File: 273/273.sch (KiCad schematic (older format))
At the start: 3 parts, among them J1 Conn_01x10_Male, J2 Conn_01x10_Male, U1 74HC273

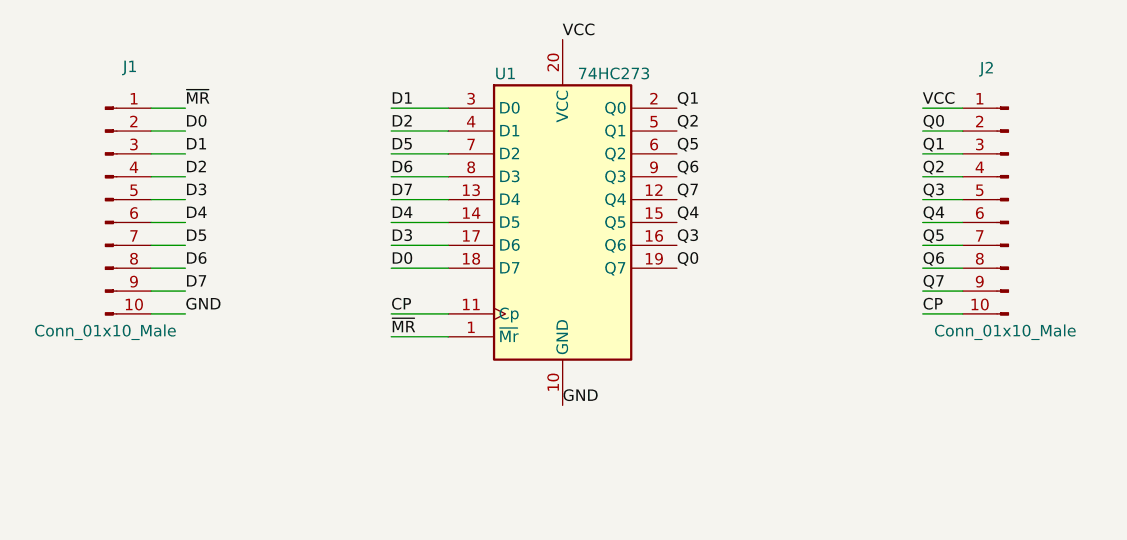
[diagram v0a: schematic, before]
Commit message: Add cap & pull-up
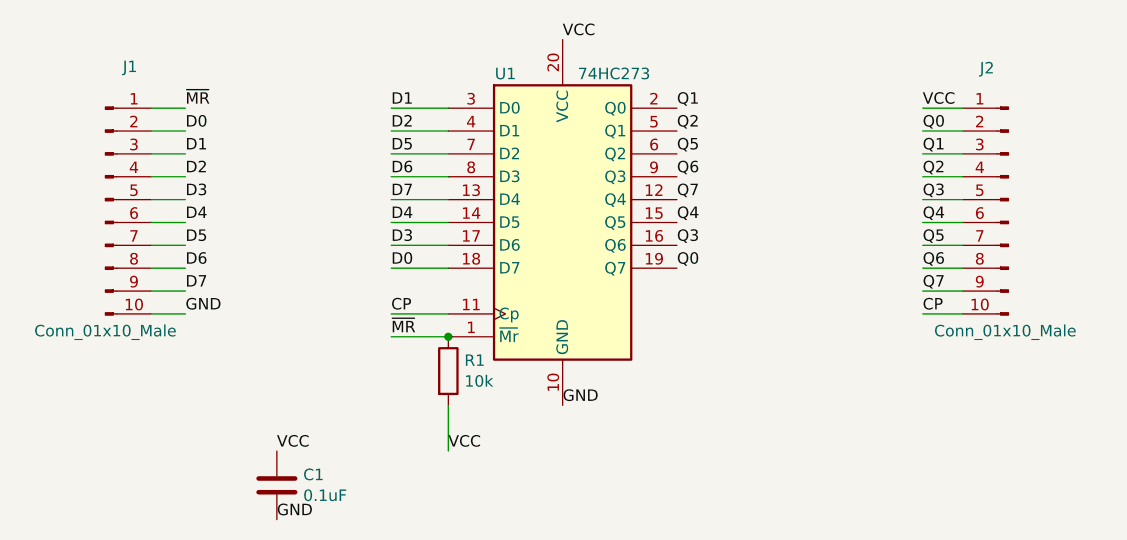
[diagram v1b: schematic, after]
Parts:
- added C1: 0.1uF, Capacitor_SMD:C_0805_2012Metric_Pad1.18x1.45mm_HandSolder, symbol Device:C
- added R1: 10k, Resistor_SMD:R_0805_2012Metric_Pad1.20x1.40mm_HandSolder, symbol Device:R
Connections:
- net GND: now also C1.2
- net VCC: now also C1.1, R1.2
- net ~MR: now also R1.1
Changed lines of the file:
@@
 Wire Wire Line
 	1450 3400 1600 3400
+$Comp
+L Device:C C1
+U 1 1 63A69FDC
+P 2000 4150
+F 0 "C1" H 2115 4196 50  0000 L CNN
+F 1 "0.1uF" H 2115 4105 50  0000 L CNN
+F 2 "Capacitor_SMD:C_0805_2012Metric_Pad1.18x1.45mm_HandSolder" H 2038 4000 50  0001 C CNN
+F 3 "~" H 2000 4150 50  0001 C CNN
+	1    2000 4150
+	1    0    0    -1
+$EndComp
+Text Label 2000 4000 0    50   ~ 0
+VCC
+Text Label 2000 4300 0    50   ~ 0
+GND
+$Comp
+L Device:R R1
+U 1 1 63A6AC8F
+P 2750 3650
+F 0 "R1" H 2820 3696 50  0000 L CNN
+F 1 "10k" H 2820 3605 50  0000 L CNN
+F 2 "Resistor_SMD:R_0805_2012Metric_Pad1.20x1.40mm_HandSolder" V 2680 3650 50  0001 C CNN
+F 3 "~" H 2750 3650 50  0001 C CNN
+	1    2750 3650
+	1    0    0    -1
+$EndComp
+Connection ~ 2750 3500
+Wire Wire Line
+	2750 4000 2750 3800
+Text Label 2750 4000 0    50   ~ 0
+VCC
 $EndSCHEMATC
